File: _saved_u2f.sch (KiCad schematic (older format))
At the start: 8 parts, among them P1 Touch Button, P2 V33prog, P3 D- prog, U1 ch552T

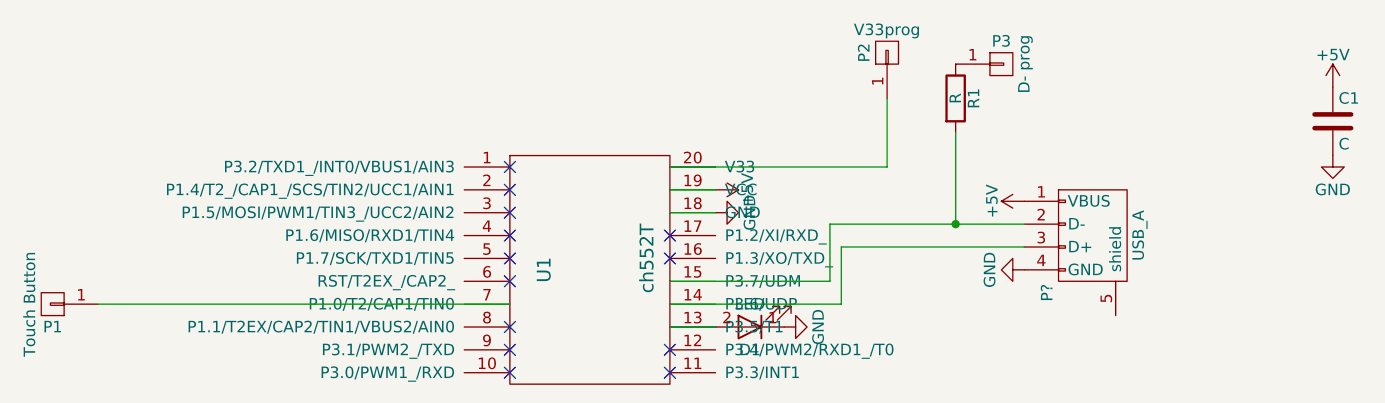
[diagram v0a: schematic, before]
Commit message: added some new footprints and stuff.
I'm having issues connecting everything up while keeping my optimal dimensions.
Options are to
- switch around some the GPIO pins (for LED) to avoid having traces run accross components
- Remove resistor and offload it to only when I'm programming (or directly wire D- and VCC to a "resistor", which will only be there during programmin)
- Remove programming pins and pre-program chip before putting it on the board (then I'd have to design a programmer PCB)
- (nucelar option) add an extra layer (basically two because I've never heard of a 3-layer PCB)
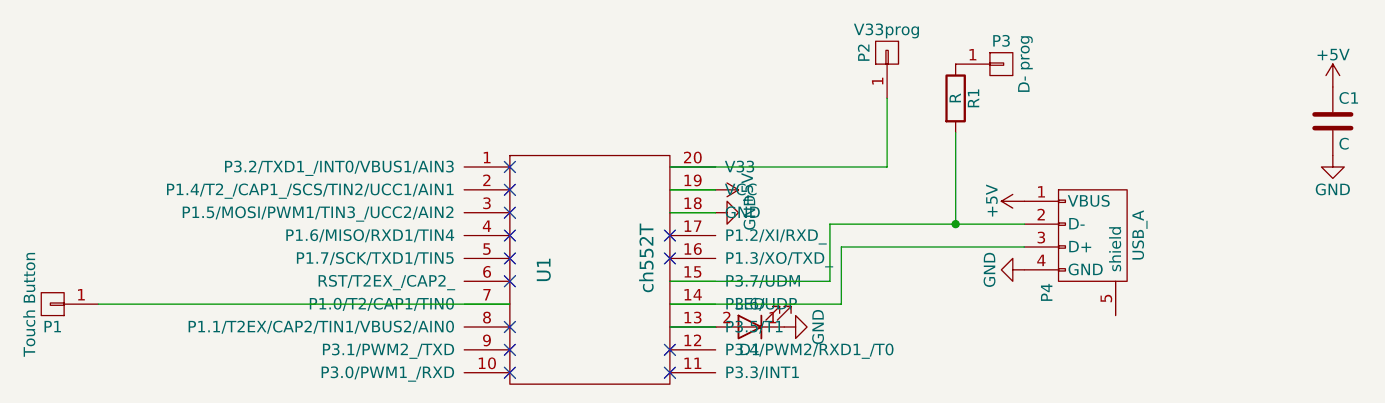
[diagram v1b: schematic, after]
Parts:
- P2, P3: footprint Wire_Pads:SolderWirePad_single_0-8mmDrill -> u2f:tp
- P4: renamed from P?; footprint (none) -> u2f:USBEdge
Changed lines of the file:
@@
 F 0 "P2" H 6600 2800 50  0000 C CNN
 F 1 "V33prog" V 6700 2700 50  0000 C CNN
-F 2 "Wire_Pads:SolderWirePad_single_0-8mmDrill" H 6600 2700 50  0001 C CNN
+F 2 "u2f:tp" H 6600 2700 50  0001 C CNN
 F 3 "" H 6600 2700 50  0000 C CNN
 	1    6600 2700
@@
 F 0 "P3" H 7100 2850 50  0000 C CNN
 F 1 "D- prog" V 7200 2750 50  0000 C CNN
-F 2 "Wire_Pads:SolderWirePad_single_0-8mmDrill" H 7100 2750 50  0001 C CNN
+F 2 "u2f:tp" H 7100 2750 50  0001 C CNN
 F 3 "" H 7100 2750 50  0000 C CNN
 	1    7100 2750
@@
 NoConn ~ 4950 4000
 $Comp
-L USB_A P?
+L USB_A P4
 U 1 1 5CF97BF4
 P 7500 3550
-F 0 "P?" H 7700 3350 50  0000 C CNN
+F 0 "P4" H 7700 3350 50  0000 C CNN
 F 1 "USB_A" H 7450 3750 50  0000 C CNN
-F 2 "" V 7450 3450 50  0000 C CNN
+F 2 "u2f:USBEdge" V 7450 3450 50  0001 C CNN
 F 3 "" V 7450 3450 50  0000 C CNN
 	1    7500 3550
